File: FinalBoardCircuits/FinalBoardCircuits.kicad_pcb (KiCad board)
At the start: 4 copper layers, 202 parts, among them IC1 SPV1040T, IC2 SPV1040T, IC3 SPV1040T, IC4 BQ25302RTER, IC5 SI3483DDV-T1-BE3, J1 Sol_X+_X-, J2 Sol_Y+_Y-, J3 Sol_Z+_Z-, J4 SWD, J5 USB_B_Micro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

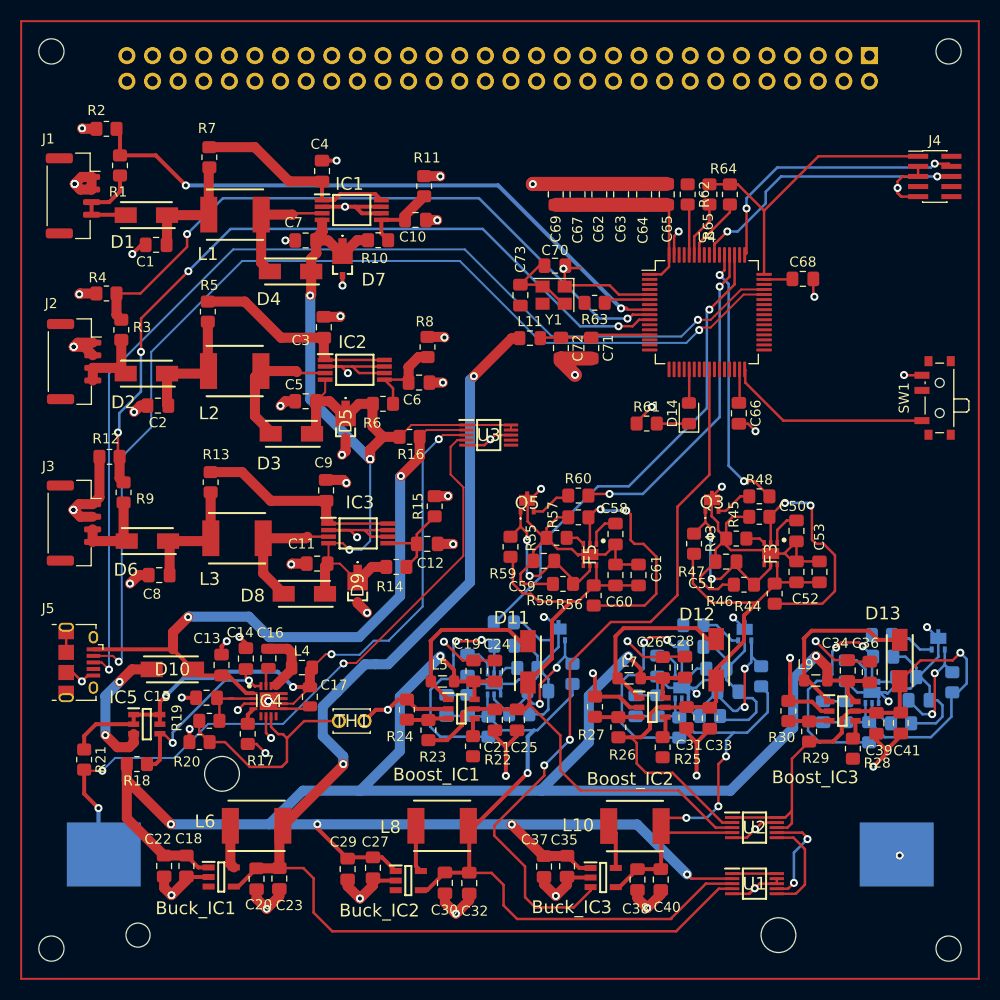
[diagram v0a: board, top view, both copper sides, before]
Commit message: Added fuel guage
Added fuel guage circuit to the final design.
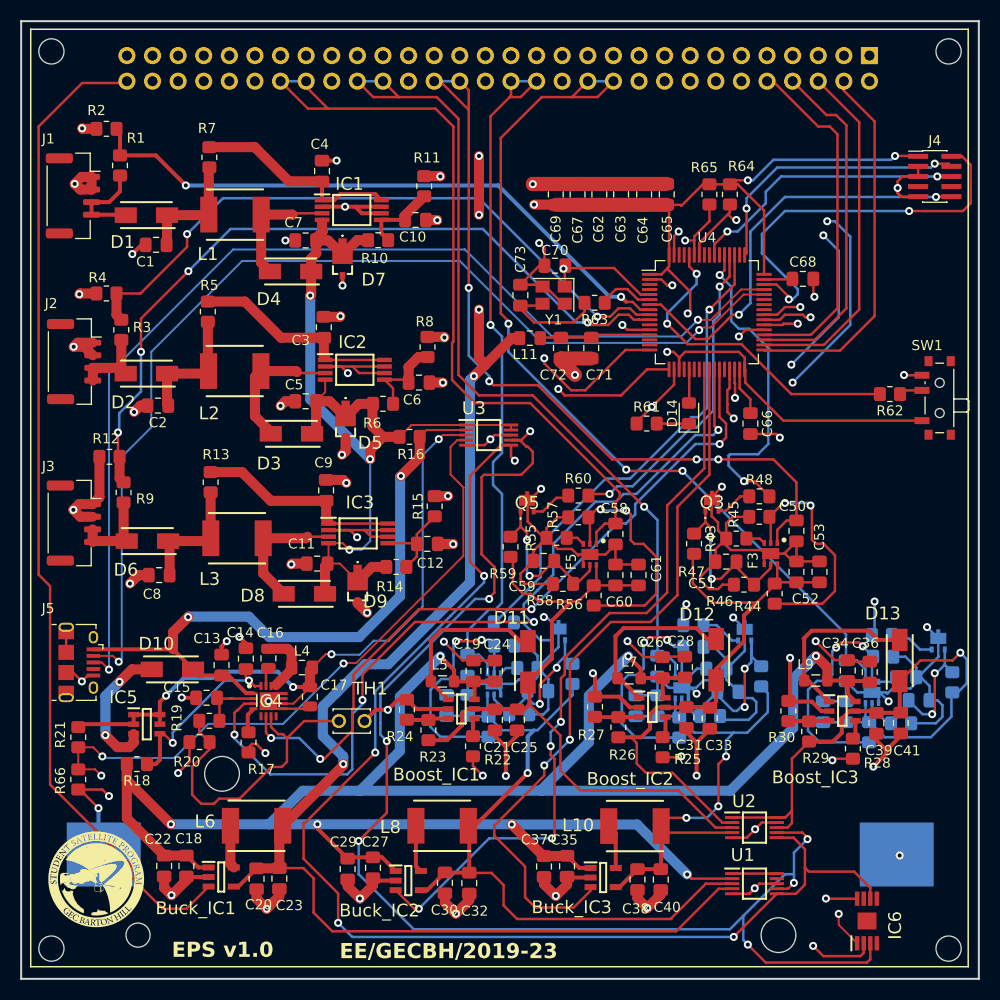
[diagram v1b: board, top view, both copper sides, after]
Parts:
- added G***: LOGO, LOGO, F.Cu at (107.4, 135.1)
- added IC6: LTC2941IMS8E#PBF, NaveenSymbols:SOP65P490X110-9N, F.Cu at (183.9, 139.3)
- added R66: 0.025, Resistor_SMD:R_0805_2012Metric_Pad1.20x1.40mm_HandSolder, F.Cu at (105.7, 125.2)
- moved R62 28.2 mm to (186.2, 87.0), turned to 180 degrees
- moved R21 2.29 mm to (105.7, 121.0)
- moved C66 1.53 mm to (172.3, 89.9)
- moved R17 0.84 mm to (122.6, 121.5)
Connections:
- BT1 pad 1: BAT_I- -> FUEL_GUAGE-
- C62 pad 2: GND -> Earth
- C63 pad 2: GND -> Earth
- C64 pad 2: GND -> Earth
- C65 pad 2: GND -> Earth
- C66 pad 2: GND -> Earth
- C67 pad 2: GND -> Earth
- C68 pad 2: GND -> Earth
- C69 pad 2: GND -> Earth
- C70 pad 2: GND -> Earth
- C71 pad 2: GND -> Earth
- C72 pad 2: GND -> Earth
- C73 pad 2: GND -> Earth
- D5 pad 3: (no net) -> MPPT_I+
- D7 pad 3: (no net) -> MPPT_I+
- D9 pad 3: (no net) -> MPPT_I+
- J4 pad 3: GND -> Earth
- J4 pad 5: GND -> Earth
- J4 pad 9: GND -> Earth
- J6 pad 10: unconnected-(J6-Pin_10-Pad10) -> SD_CARD_SPI2_MOSI
- J6 pad 13: 5Vout_COMM -> unconnected-(J6-Pin_13-Pad13)
- J6 pad 15: unconnected-(J6-Pin_15-Pad15) -> I2C2_SCL
- J6 pad 17: 5Vout_PAYLOAD -> I2C2_SDA
- J6 pad 21: 5Vout_OBC -> unconnected-(J6-Pin_21-Pad21)
- J6 pad 22: BUCK_EN_STM32 -> 5Vout_PAYLOAD
- J6 pad 24: unconnected-(J6-Pin_24-Pad24) -> 5Vout_PAYLOAD
- J6 pad 26: USART2_TX -> unconnected-(J6-Pin_26-Pad26)
- J6 pad 28: USART2_RX -> 3.3Vout_COMM
- J6 pad 30: unconnected-(J6-Pin_30-Pad30) -> 3.3Vout_COMM
- J6 pad 32: ADC_IN4 -> unconnected-(J6-Pin_32-Pad32)
- J6 pad 34: ADC_IN6 -> 5Vout_COMM
- J6 pad 36: ADC_IN7 -> 5Vout_COMM
- J6 pad 37: unconnected-(J6-Pin_37-Pad37) -> USART2_TX
- J6 pad 39: unconnected-(J6-Pin_39-Pad39) -> USART2_RX
- J6 pad 4: unconnected-(J6-Pin_4-Pad4) -> SD_CARD_SPI2_NSS
- J6 pad 40: I2C3_SDA -> 3.3Vout_ADCS
- J6 pad 42: I2C3_SCL -> 3.3Vout_ADCS
- J6 pad 46: I2C2_SDA -> 5Vout_OBC
- J6 pad 48: I2C2_SCL -> 5Vout_OBC
- J6 pad 5: 3.3Vout_COMM -> unconnected-(J6-Pin_5-Pad5)
- J6 pad 52: SD_CARD_SPI2_NSS -> unconnected-(J6-Pin_52-Pad52)
- J6 pad 53: unconnected-(J6-Pin_53-Pad53) -> Earth
- J6 pad 54: SD_CARD_SPI2_SCK -> unconnected-(J6-Pin_54-Pad54)
- J6 pad 55: unconnected-(J6-Pin_55-Pad55) -> Earth
- J6 pad 56: SD_CARD_SPI2_MISO -> unconnected-(J6-Pin_56-Pad56)
- J6 pad 57: unconnected-(J6-Pin_57-Pad57) -> Earth
- J6 pad 58: SD_CARD_SPI2_MOSI -> unconnected-(J6-Pin_58-Pad58)
- J6 pad 6: unconnected-(J6-Pin_6-Pad6) -> SD_CARD_SPI2_SCK
- J6 pad 60: unconnected-(J6-Pin_60-Pad60) -> BUCK_EN_STM32
- J6 pad 8: unconnected-(J6-Pin_8-Pad8) -> SD_CARD_SPI2_MISO
- J6 pad 9: 3.3Vout_ADCS -> unconnected-(J6-Pin_9-Pad9)
- Q1 pad 4: (no net) -> Earth
- R61 pad 1: GND -> Earth
- SW1 pad 3: GND -> Earth
- U4 pad 12: GND -> Earth
- U4 pad 18: GND -> Earth
- U4 pad 20: ADC_IN4 -> unconnected-(U4-PA4-Pad20)
- U4 pad 22: ADC_IN6 -> unconnected-(U4-PA6-Pad22)
- U4 pad 23: ADC_IN7 -> unconnected-(U4-PA7-Pad23)
- U4 pad 41: I2C3_SCL -> unconnected-(U4-PA8-Pad41)
- U4 pad 42: I2C3_SDA -> unconnected-(U4-PA9-Pad42)
- U4 pad 63: GND -> Earth
- Y1 pad 2: GND -> Earth
- Y1 pad 4: GND -> Earth
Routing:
- net I2C1_SCL: track 16.5 -> 179.0 mm, vias 2 -> 8
- net I2C1_SDA: track 15.6 -> 161.6 mm, vias 0 -> 6
- net BUCK_EN_STM32: track 0.00 -> 99.1 mm
- net FUEL_GUAGE-: track 0.00 -> 89.3 mm, vias 0 -> 3
- net 5Vout_PAYLOAD: track 3.54 -> 91.0 mm, vias 0 -> 3
- net Earth: track 442.6 -> 527.9 mm, vias 63 -> 70
- net STAT: track 1.81 -> 84.0 mm, vias 1 -> 4
- net BAT_I-: track 68.9 -> 150.1 mm, vias 3 -> 4
- net 3.3Vout_ADCS: track 3.47 -> 84.4 mm, vias 0 -> 1
- net 5Vout_COMM: track 3.59 -> 80.1 mm, vias 0 -> 4
- net 5Vout_OBC: track 3.41 -> 78.3 mm
- net BUCK_EN_COMM: track 0.00 -> 74.4 mm, vias 0 -> 4
- net BATTCH_EN: track 2.36 -> 72.4 mm, vias 1 -> 4
- net 3.3Vout_COMM: track 3.32 -> 69.9 mm, vias 0 -> 1
- net 3.3V_STM: track 192.7 -> 255.8 mm, vias 2 -> 10
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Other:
- board outline added: 95 x 95 mm
- board text added: "EE/GECBH/2019-23"
- board text added: "EPS v1.0"
